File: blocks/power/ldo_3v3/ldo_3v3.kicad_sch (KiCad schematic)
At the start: 3 parts, among them U1 HT7333 3.3V

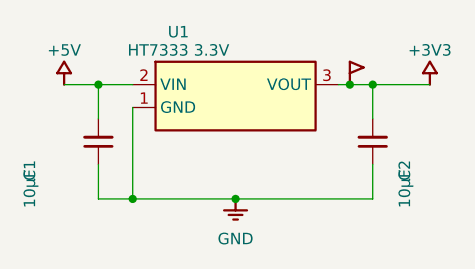
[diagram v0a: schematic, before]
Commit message: R12 최종: 표기를 자유 텍스트로 전환 — 왼쪽 정렬 고정 (사용자 지적)
'심볼 왼쪽 끝에 정렬, 삐져나오면 안 이쁘다' — 회전 심볼의 속성 텍스트는
커널이 정렬·위치를 재계산해 좌표 예측이 불가함을 실측으로 확인. 명시
배치 모드에서는 속성(Reference/Value)을 숨기고 자유 텍스트 요소로 그린다:
- 짝의 왼쪽 끝 일치 (justify left, 같은 x), 행간 2.03
- J1/U1은 심볼 왼쪽 모서리에 정렬, 수동소자는 부품 옆 좌측 정렬 열
전 게이트 PASS (블록 3개)
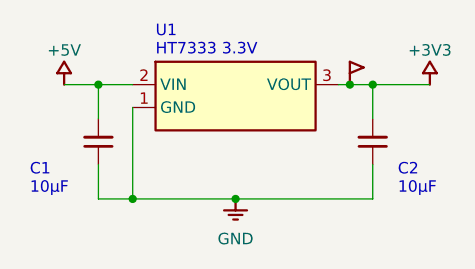
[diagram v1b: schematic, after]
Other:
- note added: "10µF"
- note added: "C1"
- note added: "C2"
- note added: "HT7333 3.3V"
- note added: "U1"
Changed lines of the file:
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@@
 		(color 0 0 0 0)
+	)
+	(text "U1"
+		(exclude_from_sim no)
+		(at 54.61 51.31 0)
+		(effects
+			(font
+				(size 1.27 1.27)
+			)
+			(justify left)
+		)
+	)
+	(text "HT7333 3.3V"
+		(exclude_from_sim no)
+		(at 54.61 53.34 0)
+		(effects
+			(font
+				(size 1.27 1.27)
+			)
+			(justify left)
+		)
+	)
+	(text "C1"
+		(exclude_from_sim no)
+		(at 40.64 66.68 0)
+		(effects
+			(font
+				(size 1.27 1.27)
+			)
+			(justify left)
+		)
+	)
+	(text "10µF"
+		(exclude_from_sim no)
+		(at 40.64 68.71 0)
+		(effects
+			(font
+				(size 1.27 1.27)
+			)
+			(justify left)
+		)
+	)
+	(text "C2"
+		(exclude_from_sim no)
+		(at 81.53 66.68 0)
+		(effects
+			(font
+				(size 1.27 1.27)
+			)
+			(justify left)
+		)
+	)
+	(text "10µF"
+		(exclude_from_sim no)
+		(at 81.53 68.71 0)
+		(effects
+			(font
+				(size 1.27 1.27)
+			)
+			(justify left)
+		)
 	)
 	(symbol
@@
 		(dnp no)
 		(property "Reference" "U1"
-			(at 57.15 51.31 0)
-			(effects
-				(font
-					(size 1.27 1.27)
-				)
+			(at 54.61 51.31 0)
+			(effects
+				(font
+					(size 1.27 1.27)
+				)
+				(hide yes)
 			)
 		)
 		(property "Value" "HT7333 3.3V"
-			(at 57.15 53.34 0)
-			(effects
-				(font
-					(size 1.27 1.27)
-				)
+			(at 54.61 53.34 0)
+			(effects
+				(font
+					(size 1.27 1.27)
+				)
+				(hide yes)
 			)
 		)
@@
 					(size 1.27 1.27)
 				)
+				(hide yes)
 			)
 		)
@@
 					(size 1.27 1.27)
 				)
+				(hide yes)
 			)
 		)
@@
 		(dnp no)
 		(property "Reference" "C2"
-			(at 82.3 66.68 0)
-			(effects
-				(font
-					(size 1.27 1.27)
-				)
+			(at 81.53 66.68 0)
+			(effects
+				(font
+					(size 1.27 1.27)
+				)
+				(hide yes)
 			)
 		)
 		(property "Value" "10µF"
-			(at 82.3 68.71 0)
-			(effects
-				(font
-					(size 1.27 1.27)
-				)
-			)
-		)
+			(at 81.53 68.71 0)
+			(effects
+				(font
+					(size 1.27 1.27)
+				)
+				(hide yes)
+			)
+		)
